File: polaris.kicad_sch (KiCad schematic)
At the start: 23 parts, among them J101 XT60-M, J102 SPI, J103 I2C, J104 PB, J105 SWD, J106 PYRO5, J107 PYRO4, J108 PYRO3, J109 PYRO2, J110 PYRO1, J111 PYRO0, J112 SERVO0, J113 SERVO1, J114 SERVO2, J115 SERVO3, J116 SERVO4, J117 SERVO5, J118 RADIO, J119 POWER

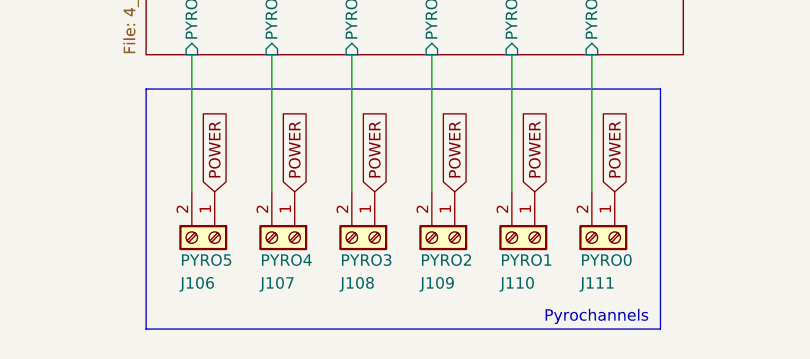
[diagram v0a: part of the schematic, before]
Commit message: Major changes
Updated schematic for better power delivery
Changed 3.3V supply to buck converter instead of LDO due to heat
Deleted the entire PCB, redoing the whole thing due to problems in
laying traces that made some connections impossible to make
Also updated README to reflect these changes
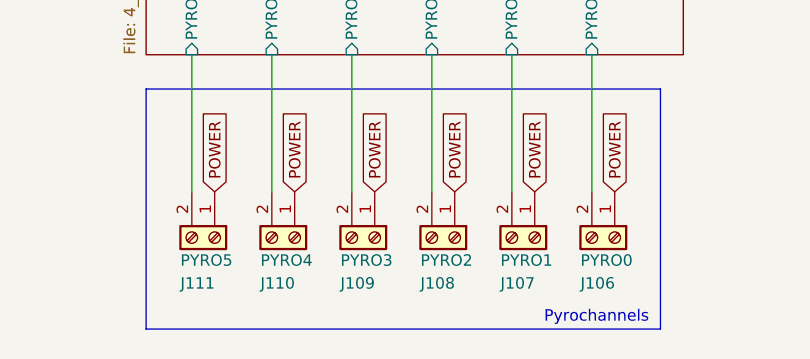
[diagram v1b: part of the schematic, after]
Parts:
- renumbered J111 to J106, J110 to J107, J109 to J108, J108 to J109, J107 to J110, J106 to J111
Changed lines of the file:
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@@
 		(in_pos_files yes)
 		(dnp no)
-		(property "Reference" "J106"
+		(property "Reference" "J111"
 			(at 114.3 189.23 90)
 			(show_name no)
@@
 			(project "polaris"
 				(path "/cfb90e19-9fbe-47a1-a5ac-df522853d1d0"
-					(reference "J106")
+					(reference "J111")
 					(unit 1)
 				)
@@
 		(in_pos_files yes)
 		(dnp no)
-		(property "Reference" "J110"
+		(property "Reference" "J107"
 			(at 149.86 189.23 90)
 			(show_name no)
@@
 			(project "polaris"
 				(path "/cfb90e19-9fbe-47a1-a5ac-df522853d1d0"
-					(reference "J110")
+					(reference "J107")
 					(unit 1)
 				)
@@
 		(in_pos_files yes)
 		(dnp no)
-		(property "Reference" "J111"
+		(property "Reference" "J106"
 			(at 158.75 189.23 90)
 			(show_name no)
@@
 			(project "polaris"
 				(path "/cfb90e19-9fbe-47a1-a5ac-df522853d1d0"
-					(reference "J111")
+					(reference "J106")
 					(unit 1)
 				)
@@
 		(in_pos_files yes)
 		(dnp no)
-		(property "Reference" "J107"
+		(property "Reference" "J110"
 			(at 123.19 189.23 90)
 			(show_name no)
@@
 			(project "polaris"
 				(path "/cfb90e19-9fbe-47a1-a5ac-df522853d1d0"
-					(reference "J107")
+					(reference "J110")
 					(unit 1)
 				)
@@
 		(in_pos_files yes)
 		(dnp no)
-		(property "Reference" "J108"
+		(property "Reference" "J109"
 			(at 132.08 189.23 90)
 			(show_name no)
@@
 			(project "polaris"
 				(path "/cfb90e19-9fbe-47a1-a5ac-df522853d1d0"
-					(reference "J108")
+					(reference "J109")
 					(unit 1)
 				)
@@
 		(in_pos_files yes)
 		(dnp no)
-		(property "Reference" "J109"
+		(property "Reference" "J108"
 			(at 140.97 189.23 90)
 			(show_name no)
@@
 			(project "polaris"
 				(path "/cfb90e19-9fbe-47a1-a5ac-df522853d1d0"
-					(reference "J109")
+					(reference "J108")
 					(unit 1)
 				)

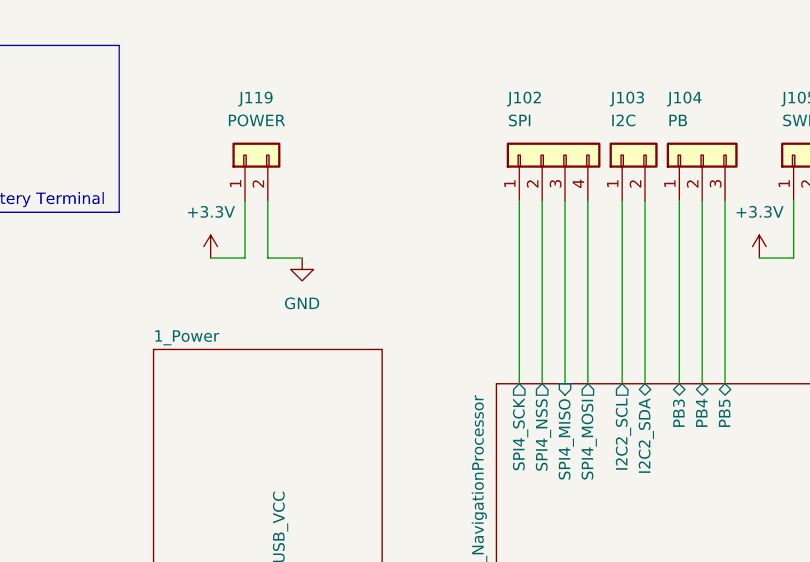
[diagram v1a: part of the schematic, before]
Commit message: Finished most of component re-placement
Began laying tracks for important connections
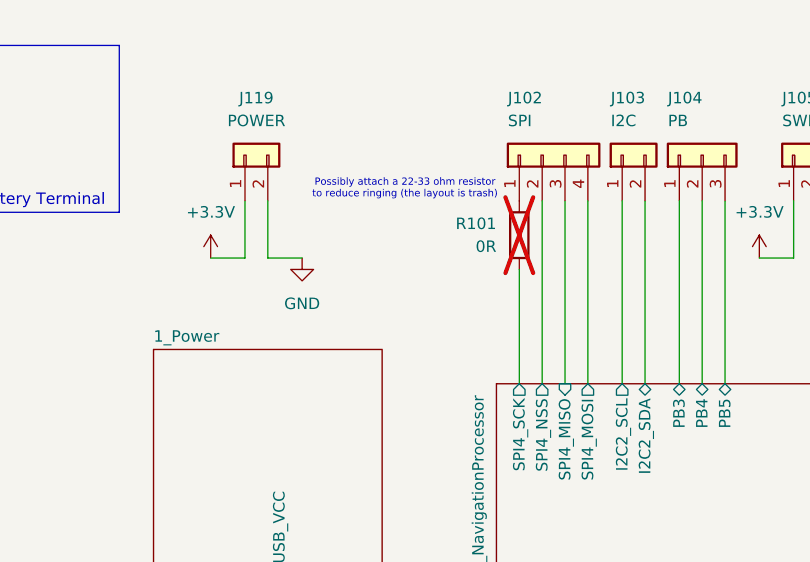
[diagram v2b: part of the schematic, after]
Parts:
- added R101: 0R, Resistor_SMD:R_0603_1608Metric, symbol Device:R
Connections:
- net 3_NavigationProcessor/SPI4_SCK: now also R101.2; no longer J102.1 (Pin_1)
- new net: J102.1 (Pin_1), R101.1
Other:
- note added: "Possibly attach a 22-33 ohm resistor to reduce ringing (the layout is trash)"
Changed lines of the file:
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@@
 		)
 	)
+	(text "Possibly attach a 22-33 ohm resistor\nto reduce ringing (the layout is trash)"
+		(exclude_from_sim no)
+		(at 100.33 33.02 0)
+		(effects
+			(font
+				(face "Segoe UI Symbol")
+				(size 0.8 0.8)
+			)
+		)
+	)
 	(text "Servo Line 4"
 		(exclude_from_sim no)
@@
 	(wire
 		(pts
-			(xy 113.03 34.29) (xy 113.03 54.61)
+			(xy 85.09 40.64) (xy 88.9 40.64)
 		)
 		(stroke
@@
 	(wire
 		(pts
-			(xy 85.09 40.64) (xy 88.9 40.64)
+			(xy 113.03 41.91) (xy 113.03 54.61)
 		)
 		(stroke
@@
 					(unit 1)
 				)
+			)
+		)
+	)
+	(symbol
+		(lib_id "Device:R")
+		(at 113.03 38.1 0)
+		(unit 1)
+		(body_style 1)
+		(exclude_from_sim no)
+		(in_bom yes)
+		(on_board yes)
+		(in_pos_files yes)
+		(dnp yes)
+		(property "Reference" "R101"
+			(at 110.49 36.8299 0)
+			(show_name no)
+			(do_not_autoplace no)
+			(effects
+				(font
+					(size 1.27 1.27)
+				)
+				(justify right)
+			)
+		)
+		(property "Value" "0R"
+			(at 110.49 39.3699 0)
+			(show_name no)
+			(do_not_autoplace no)
+			(effects
+				(font
+					(size 1.27 1.27)
+				)
+				(justify right)
+			)
+		)
+		(property "Footprint" "Resistor_SMD:R_0603_1608Metric"
+			(at 111.252 38.1 90)
+			(hide yes)
+			(show_name no)
+			(do_not_autoplace no)
+			(effects
+				(font
+					(size 1.27 1.27)
+				)
+			)
+		)
+		(property "Datasheet" ""
+			(at 113.03 38.1 0)
+			(hide yes)
+			(show_name no)
+			(do_not_autoplace no)
+			(effects
+				(font
+					(size 1.27 1.27)
+				)
+			)
+		)
+		(property "Description" "Resistor"
+			(at 113.03 38.1 0)
+			(hide yes)
+			(show_name no)
+			(do_not_autoplace no)
+			(effects
+				(font
+					(size 1.27 1.27)
+				)
+			)
+		)
+		(pin "2"
+		)
+		(pin "1"
+		)
+		(instances
+			(project "polaris"
+				(path "/cfb90e19-9fbe-47a1-a5ac-df522853d1d0"
+					(reference "R101")
+					(unit 1)
+				)

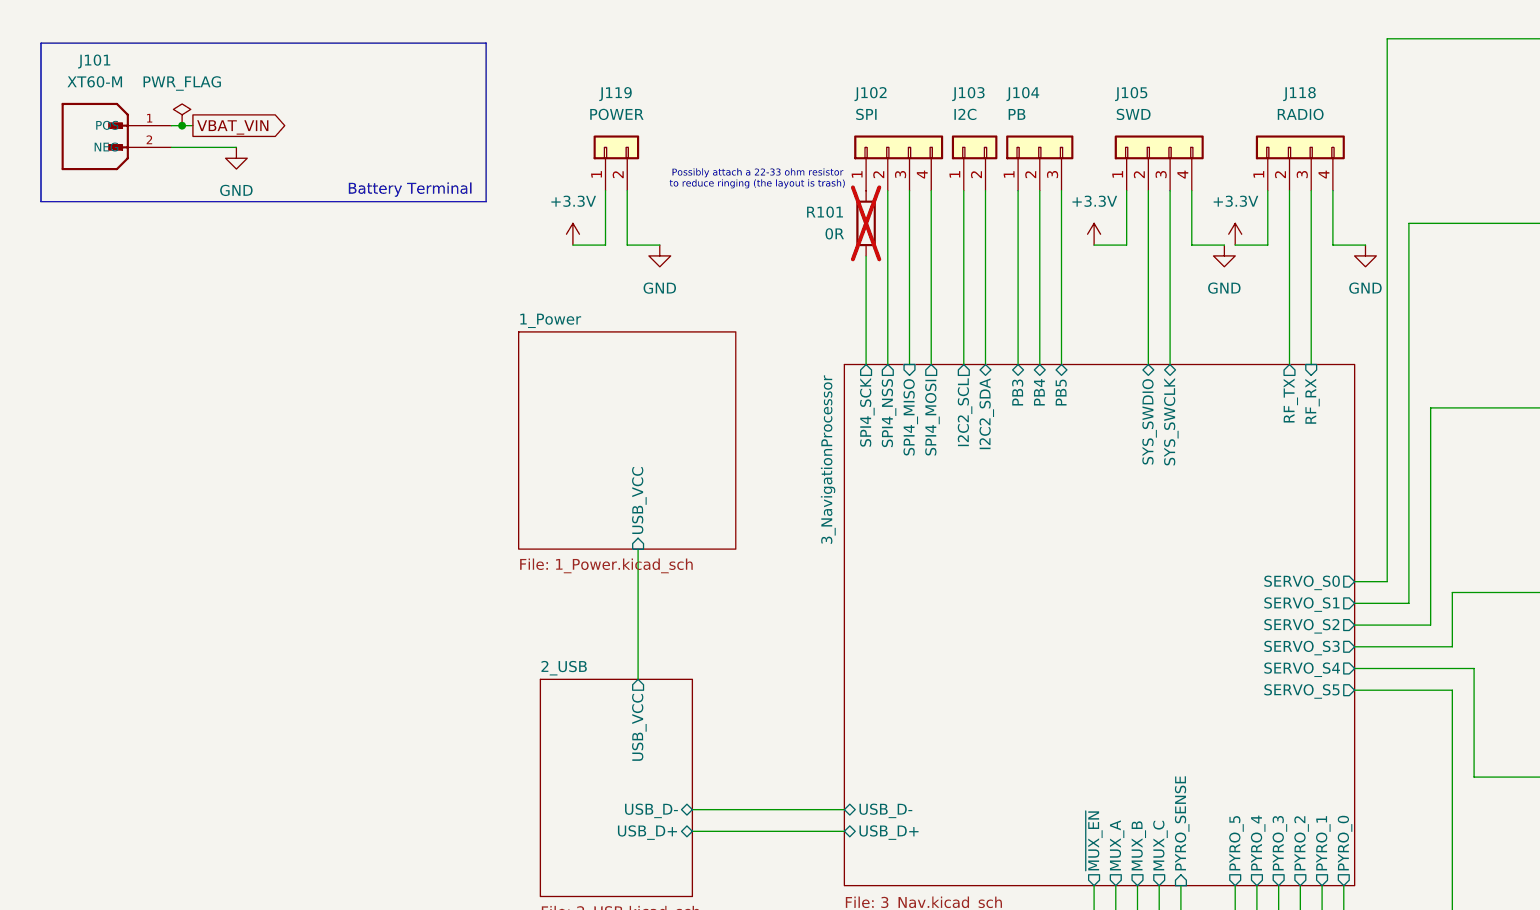
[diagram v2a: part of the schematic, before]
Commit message: Added more power (3.3V) headers for more powering peripherals
Continued laying out tracks
Revised order of connections to pyrochannel mux for easier routing
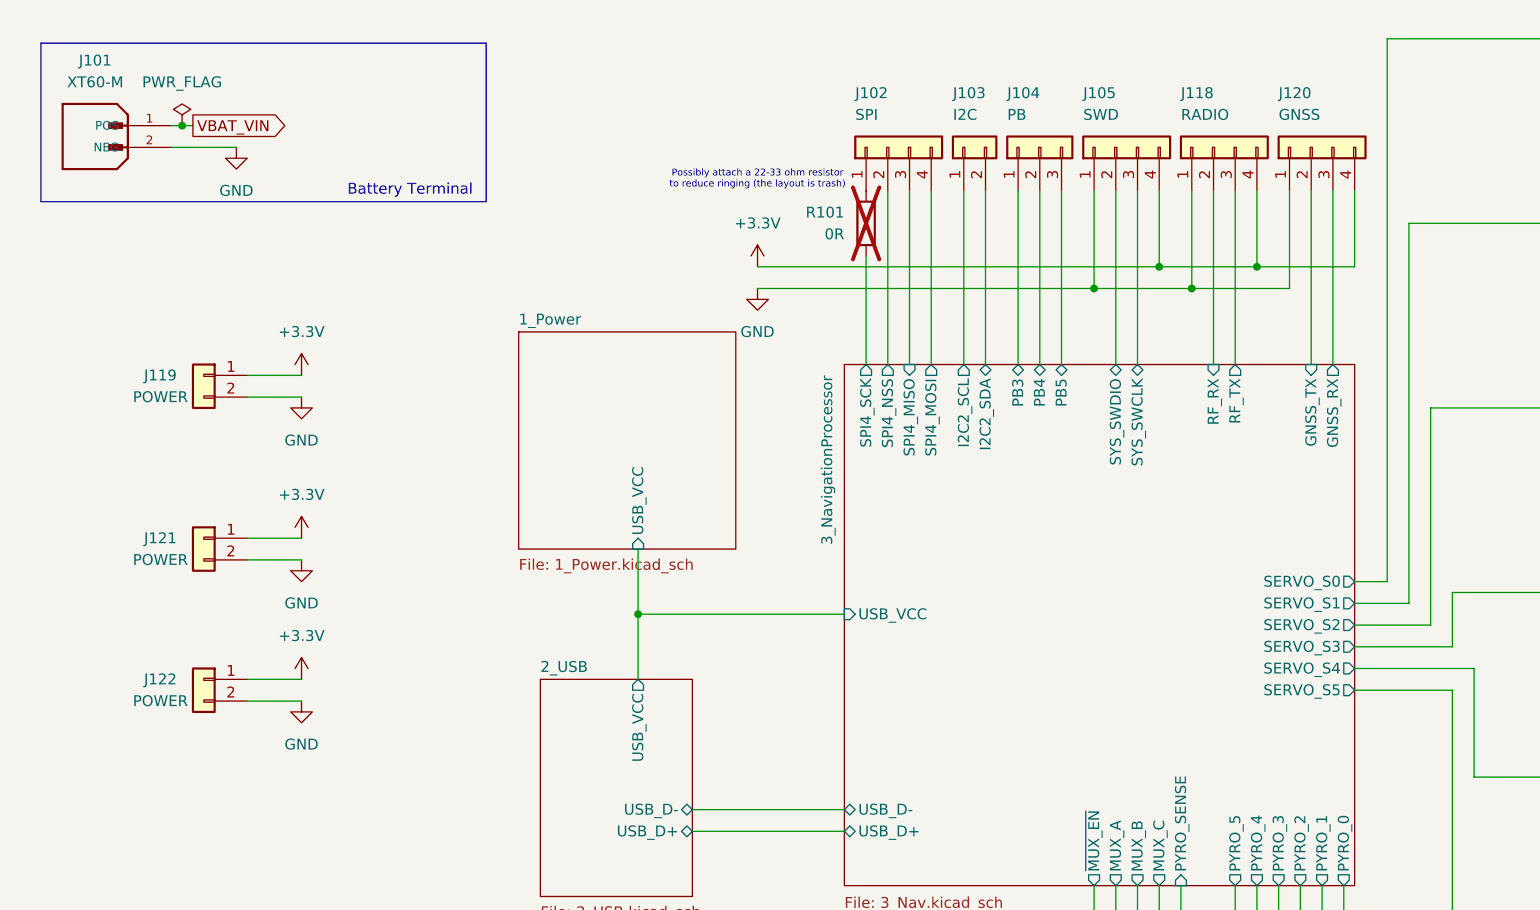
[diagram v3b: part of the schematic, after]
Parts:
- added J120: GNSS, Connector_JST:JST_XH_B4B-XH-A_1x04_P2.50mm_Vertical, symbol Connector_Generic:Conn_01x04
- added J121, J122: POWER, TerminalBlock:TerminalBlock_Xinya_XY308-2.54-2P_1x02_P2.54mm_Horizontal, symbol Connector_Generic:Conn_01x02
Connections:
- net +3.3V: now also J105.4 (Pin_4), J118.4 (Pin_4), J120.4 (Pin_4), J121.1 (Pin_1), J122.1 (Pin_1); no longer J105.1 (Pin_1), J118.1 (Pin_1)
- net 3_NavigationProcessor/RF_RX: now also J118.2 (Pin_2); no longer J118.3 (Pin_3)
- net 3_NavigationProcessor/RF_TX: now also J118.3 (Pin_3); no longer J118.2 (Pin_2)
- net GND: now also J105.1 (Pin_1), J118.1 (Pin_1), J120.1 (Pin_1), J121.2 (Pin_2), J122.2 (Pin_2); no longer J105.4 (Pin_4), J118.4 (Pin_4)
- new net 3_NavigationProcessor/GNSS_RX: J120.3 (Pin_3)
- new net 3_NavigationProcessor/GNSS_TX: J120.2 (Pin_2)
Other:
- sheet 3_NavigationProcessor ports: added GNSS_RX, GNSS_TX, USB_VCC; removed none
- moved on the sheet: J105, J118
